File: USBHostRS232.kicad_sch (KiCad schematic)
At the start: 50 parts, among them J1 Conn_01x10_Male, J2 DB9_Male, J3 DB9_Male, J4 USB_A, J5 5V_IN, Q1 SI2301CDS-T1-GE3, SW1 PROG, SW2 RST, U1 MAX3232, U2 CH559L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

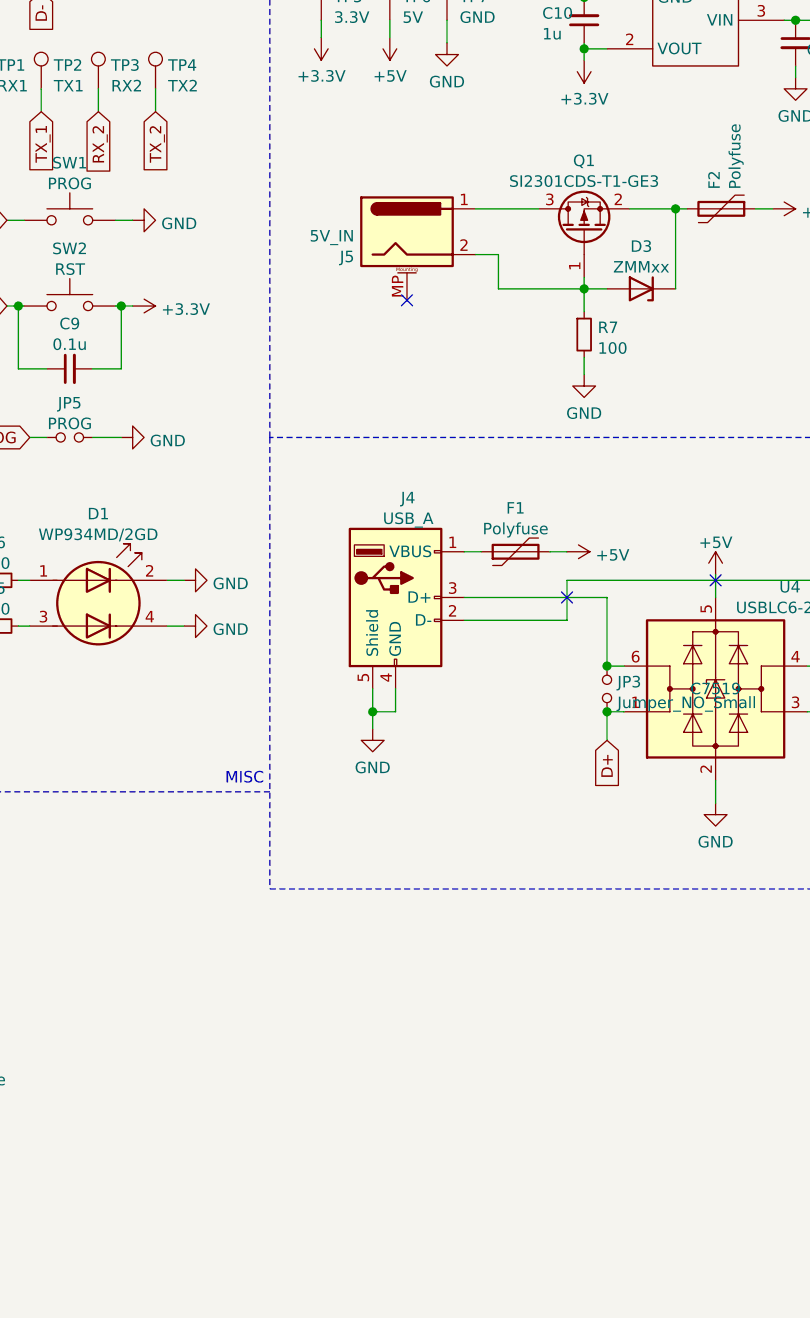
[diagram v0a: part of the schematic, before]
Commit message: Added mounting holes
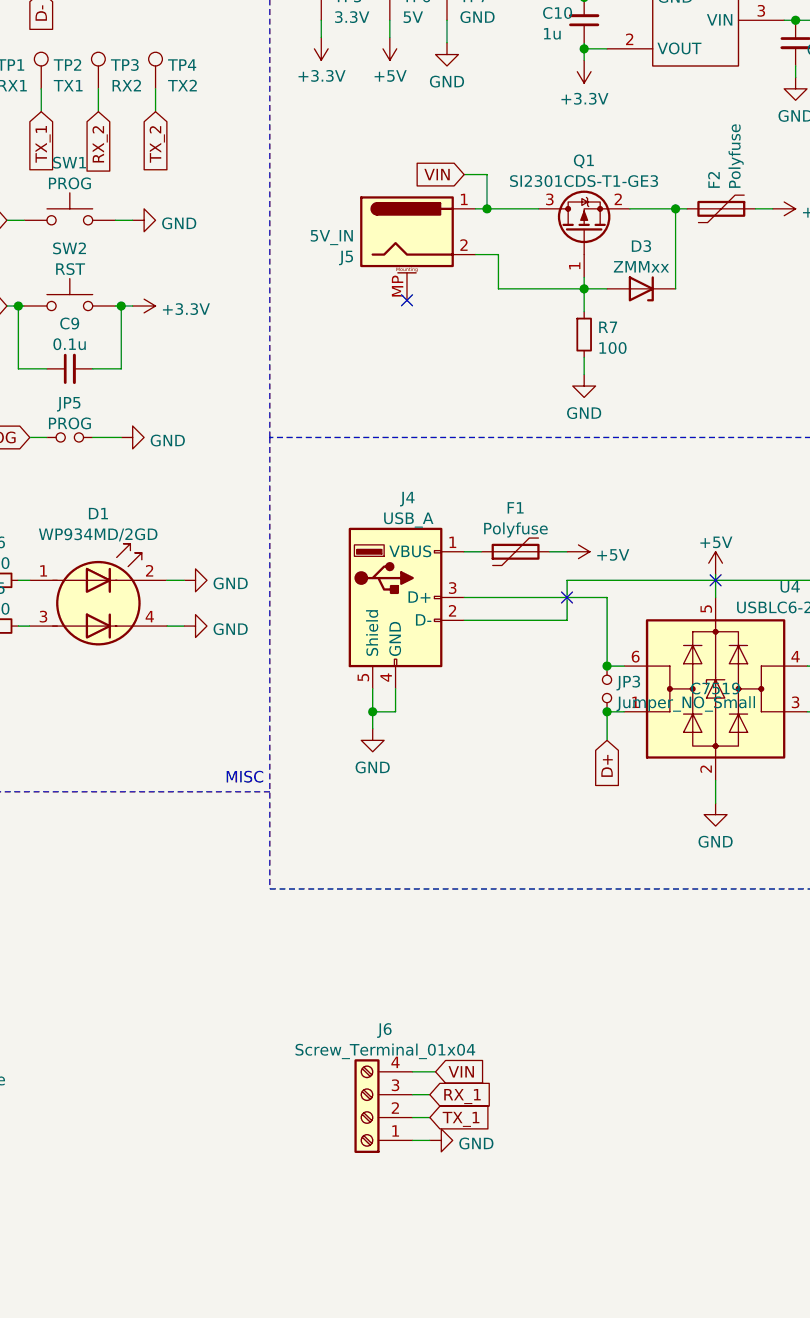
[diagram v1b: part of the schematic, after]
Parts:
- added J6: Screw_Terminal_01x04, TerminalBlock_Phoenix:TerminalBlock_Phoenix_MKDS-1,5-4-5.08_1x04_P5.08mm_Horizontal, symbol Connector:Screw_Terminal_01x04
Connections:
- net GND: now also J6.1 (Pin_1)
- net RX_1: now also J6.3 (Pin_3)
- net TX_1: now also J6.2 (Pin_2)
- net VIN: now reaches J5.1, Q1.3 (D)
- net VIN: now also J6.4 (Pin_4)
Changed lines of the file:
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@@
   (junction (at 182.88 57.15) (diameter 1.016) (color 0 0 0 0))
   (junction (at 210.82 102.235) (diameter 1.016) (color 0 0 0 0))
+  (junction (at 223.52 46.355) (diameter 1.016) (color 0 0 0 0))
   (junction (at 234.315 22.86) (diameter 1.016) (color 0 0 0 0))
   (junction (at 234.315 28.575) (diameter 1.016) (color 0 0 0 0))
@@
     (stroke (width 0) (type solid) (color 0 0 0 0))
   )
+  (wire (pts (xy 215.265 142.24) (xy 217.805 142.24))
+    (stroke (width 0) (type solid) (color 0 0 0 0))
+  )
+  (wire (pts (xy 215.265 144.78) (xy 217.17 144.78))
+    (stroke (width 0) (type solid) (color 0 0 0 0))
+  )
+  (wire (pts (xy 215.265 147.32) (xy 217.17 147.32))
+    (stroke (width 0) (type solid) (color 0 0 0 0))
+  )
+  (wire (pts (xy 215.265 149.86) (xy 217.17 149.86))
+    (stroke (width 0) (type solid) (color 0 0 0 0))
+  )
   (wire (pts (xy 219.075 25.4) (xy 219.075 27.94))
     (stroke (width 0) (type solid) (color 0 0 0 0))
   )
+  (wire (pts (xy 220.98 42.545) (xy 223.52 42.545))
+    (stroke (width 0) (type solid) (color 0 0 0 0))
+  )
   (wire (pts (xy 220.98 84.455) (xy 222.885 84.455))
     (stroke (width 0) (type solid) (color 0 0 0 0))
@@
     (stroke (width 0) (type solid) (color 0 0 0 0))
   )
-  (wire (pts (xy 222.25 46.355) (xy 229.235 46.355))
+  (wire (pts (xy 222.25 46.355) (xy 223.52 46.355))
     (stroke (width 0) (type solid) (color 0 0 0 0))
   )
   (wire (pts (xy 222.25 51.435) (xy 224.79 51.435))
+    (stroke (width 0) (type solid) (color 0 0 0 0))
+  )
+  (wire (pts (xy 223.52 42.545) (xy 223.52 46.355))
+    (stroke (width 0) (type solid) (color 0 0 0 0))
+  )
+  (wire (pts (xy 223.52 46.355) (xy 229.235 46.355))
     (stroke (width 0) (type solid) (color 0 0 0 0))
   )
@@
     (effects (font (size 1.27 1.27)) (justify right))
     (property "Intersheet References" "${INTERSHEET_REFS}" (id 0) (at 186.6106 42.3274 90)
+      (effects (font (size 1.27 1.27)) (justify right) hide)
+    )
+  )
+  (global_label "RX_1" (shape input) (at 217.17 144.78 0)
+    (effects (font (size 1.27 1.27)) (justify left))
+    (property "Intersheet References" "${INTERSHEET_REFS}" (id 0) (at 224.2398 144.8594 0)
+      (effects (font (size 1.27 1.27)) (justify left) hide)
+    )
+  )
+  (global_label "TX_1" (shape input) (at 217.17 147.32 0)
+    (effects (font (size 1.27 1.27)) (justify left))
+    (property "Intersheet References" "${INTERSHEET_REFS}" (id 0) (at 223.9374 147.3994 0)
+      (effects (font (size 1.27 1.27)) (justify left) hide)
+    )
+  )
+  (global_label "VIN" (shape input) (at 217.805 142.24 0) (fields_autoplaced)
+    (effects (font (size 1.27 1.27)) (justify left))
+    (property "Intersheet References" "${INTERSHEET_REFS}" (id 0) (at 223.2419 142.3194 0)
+      (effects (font (size 1.27 1.27)) (justify left) hide)
+    )
+  )
+  (global_label "VIN" (shape input) (at 220.98 42.545 180) (fields_autoplaced)
+    (effects (font (size 1.27 1.27)) (justify right))
+    (property "Intersheet References" "${INTERSHEET_REFS}" (id 0) (at 215.5431 42.4656 0)
       (effects (font (size 1.27 1.27)) (justify right) hide)
     )
@@
     (pin "1")
   )
+  (symbol (lib_id "power:GND") (at 217.17 149.86 90) (unit 1)
+    (in_bom yes) (on_board yes) (fields_autoplaced)
+    (property "Reference" "#PWR0135" (id 0) (at 223.52 149.86 0)
+      (effects (font (size 1.27 1.27)) hide)
+    )
+    (property "Value" "GND" (id 1) (at 220.3451 150.2485 90)
+      (effects (font (size 1.27 1.27)) (justify right))
+    )
+    (property "Footprint" "" (id 2) (at 217.17 149.86 0)
+      (effects (font (size 1.27 1.27)) hide)
+    )
+    (property "Datasheet" "" (id 3) (at 217.17 149.86 0)
+      (effects (font (size 1.27 1.27)) hide)
+    )
+    (pin "1")
+  )
   (symbol (lib_id "power:GND") (at 219.075 27.94 0) (unit 1)
     (in_bom yes) (on_board yes)
@@
     (pin "1")
     (pin "2")
+  )
+  (symbol (lib_id "Connector:Screw_Terminal_01x04") (at 210.185 147.32 180) (unit 1)
+    (in_bom yes) (on_board yes) (fields_autoplaced)
+    (property "Reference" "J6" (id 0) (at 212.217 137.5368 0))
+    (property "Value" "Screw_Terminal_01x04" (id 1) (at 212.217 139.8355 0))
+    (property "Footprint" "TerminalBlock_Phoenix:TerminalBlock_Phoenix_MKDS-1,5-4-5.08_1x04_P5.08mm_Horizontal" (id 2) (at 210.185 147.32 0)
+      (effects (font (size 1.27 1.27)) hide)
+    )
+    (property "Datasheet" "~" (id 3) (at 210.185 147.32 0)
+      (effects (font (size 1.27 1.27)) hide)
+    )
+    (pin "1")
+    (pin "2")
+    (pin "3")
+    (pin "4")
   )
   (symbol (lib_id "Device:Q_PMOS_GSD") (at 234.315 48.895 90) (unit 1)
@@
       (reference "#PWR0134") (unit 1) (value "GND") (footprint "")
     )
+    (path "/7a8ab882-6aac-4298-bbae-e27d433fa9ef"
+      (reference "#PWR0135") (unit 1) (value "GND") (footprint "")
+    )
     (path "/57bdc261-5efd-4af3-b53c-65cae2bf1e61"
       (reference "C1") (unit 1) (value "1u") (footprint "Capacitor_SMD:C_0603_1608Metric")
@@
       (reference "J5") (unit 1) (value "5V_IN") (footprint "Connector_BarrelJack:BarrelJack_CUI_PJ-063AH_Horizontal")
     )
+    (path "/c64f87ef-894c-42c2-ab72-4917f29df872"
+      (reference "J6") (unit 1) (value "Screw_Terminal_01x04") (footprint "TerminalBlock_Phoenix:TerminalBlock_Phoenix_MKDS-1,5-4-5.08_1x04_P5.08mm_Horizontal")
+    )
     (path "/0cd78026-47ce-4bbb-a215-f7575c9fd56f"
